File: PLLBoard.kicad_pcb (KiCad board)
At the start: 2 copper layers, 41.1 x 27.9 mm, 28 parts, among them J1 Conn_01x07, J2 Conn_Coaxial, J3 Conn_Coaxial, J4 Conn_Coaxial, Q1 2N7002, Q2 2N7002, U1 AMS1117-3.3, U2 Si5351A-B-GT, Y1 25 MHz, Y2 25 MHz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

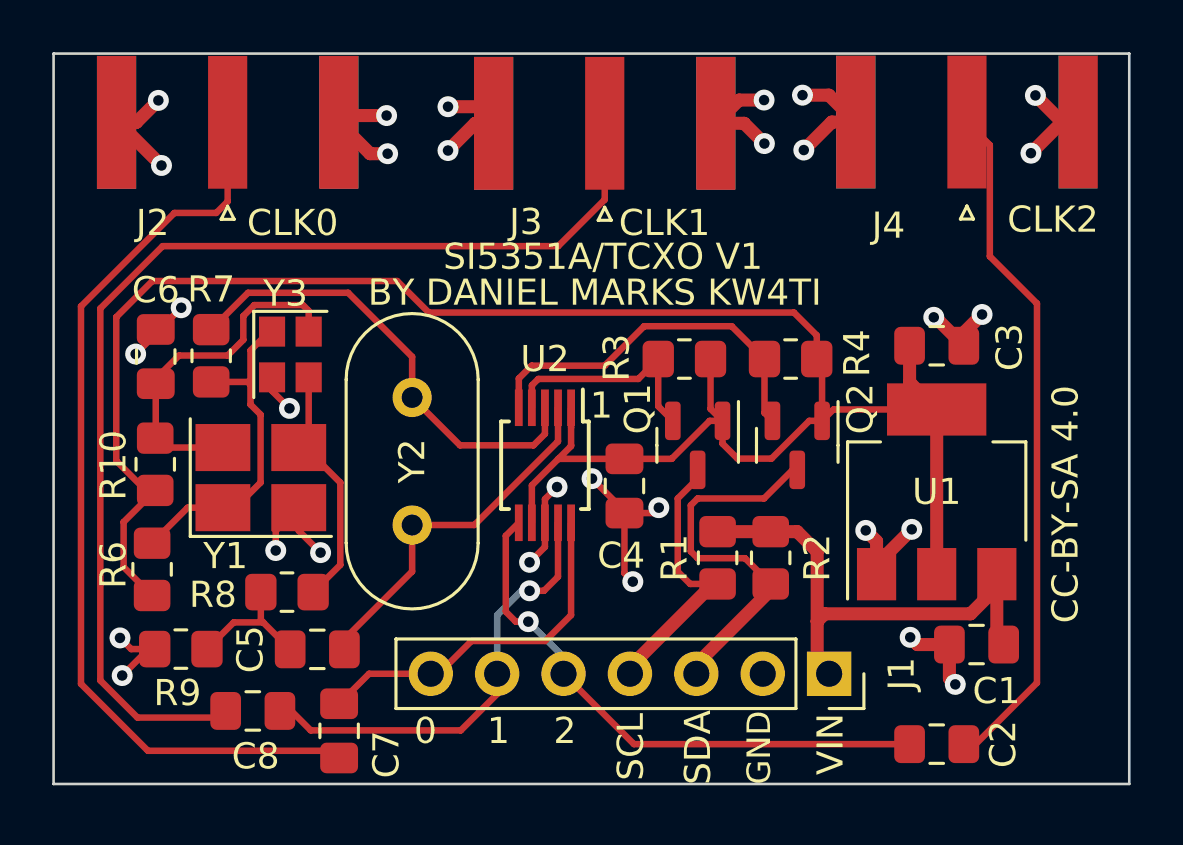
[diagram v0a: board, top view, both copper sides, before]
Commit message: Shrink PLL board, remove resistor
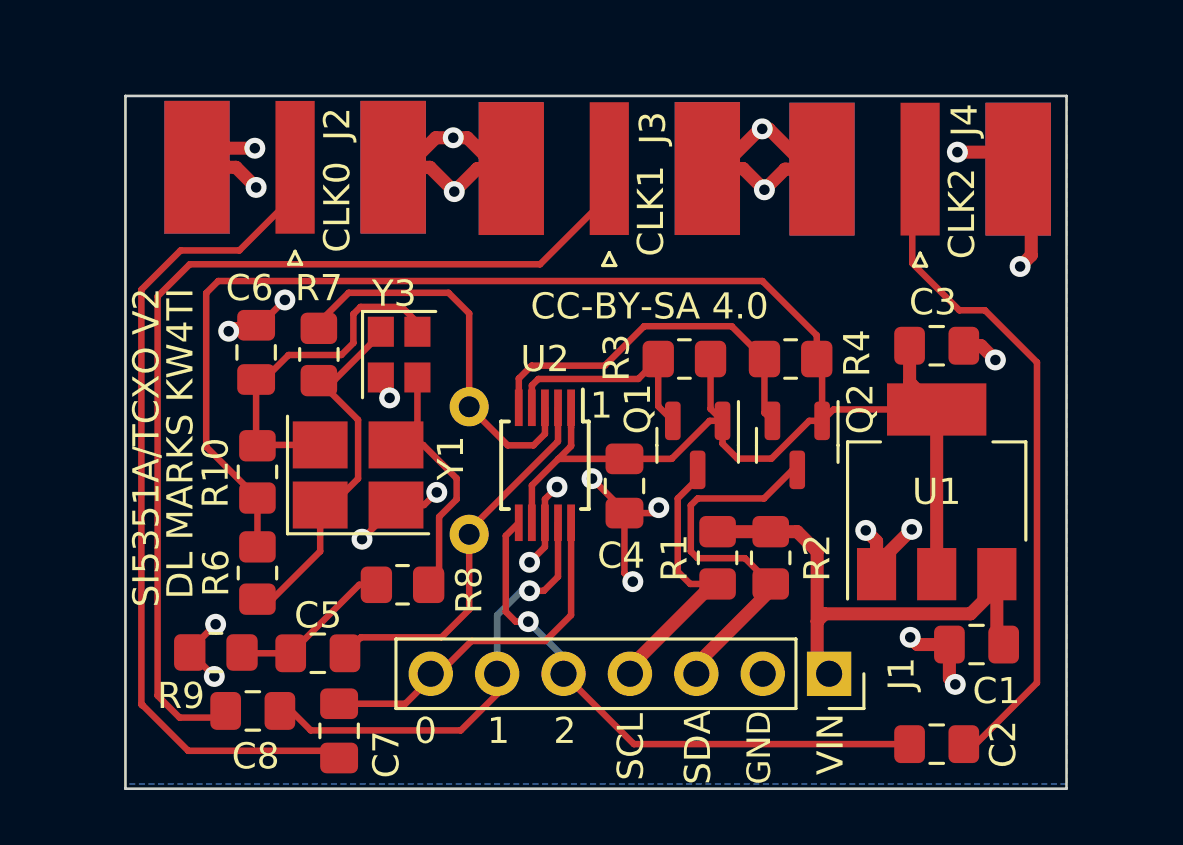
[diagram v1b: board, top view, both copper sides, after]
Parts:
- J2, J3, J4: footprint Connector_Coaxial:SMA_Amphenol_132289_EdgeMount -> PLLBoard:SMA_Amphenol_132289_EdgeMount_Wide
- R10: value 0R -> NC
- Y2: moved to B.Cu
- moved R8 4.43 mm to (61.1, 76.2)
- moved Y3 4.16 mm to (61.0, 67.4)
- moved R7 4.12 mm to (57.9, 67.4)
- moved R6 4.03 mm to (55.5, 75.8), turned to -90 degrees
- moved R10 3.92 mm to (55.5, 71.9)
- moved C6 3.84 mm to (55.5, 67.3)
- moved Y1 3.72 mm to (59.4, 72.0)
- moved J2 3.10 mm to (57.0, 60.2)
- moved J4 2.54 mm to (80.9, 60.3)
- moved Y2 2.21 mm to (63.6, 74.3)
- moved J3 1.74 mm to (69.0, 60.3)
- moved R9 1.35 mm to (54.0, 78.8)
- moved C5 0.15 mm to (57.9, 78.8)
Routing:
- net +3V3: track 77.7 -> 72.0 mm
- net Net-(C8-Pad1): track 43.7 -> 38.2 mm
- net Net-(C7-Pad1): track 35.8 -> 32.7 mm
- net Net-(R7-Pad1): track 17.9 -> 15.0 mm
- net Net-(R6-Pad2): track 13.0 -> 15.6 mm
- net GND: track 56.9 -> 58.6 mm, vias 30 -> 25
- net Net-(C5-Pad1): track 5.23 -> 6.24 mm
- net Net-(R8-Pad2): track 9.61 -> 10.3 mm
- net Net-(C5-Pad2): track 14.0 -> 14.6 mm
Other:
- board size 41.1 x 27.9 mm -> 36 x 26.5 mm
- board text added: "DL MARKS KW4TI"
- board text added: "SI5351A/TCXO V2"
- board text removed: "BY DANIEL MARKS KW4TI"
- board text removed: "SI5351A/TCXO V1"
